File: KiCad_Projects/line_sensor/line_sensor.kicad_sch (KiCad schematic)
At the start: 4 parts, among them J1 Conn_01x05_Female, U1 S4282-51, U2 S4282-51

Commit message: 基盤データのアップデート
ローカルコミットはちゃんと作ってください
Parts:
- removed J1: Conn_01x05_Female, Connector_PinHeader_2.54mm:PinHeader_1x05_P2.54mm_Vertical, symbol Connector:Conn_01x05_Female
- added C1: (no value), symbol Device:C_Small
- added C10, C11, C12, C13, C14, C15, C16, C2, C3, C4, C5, C6, C7, C8, C9: C_Small, symbol Device:C_Small
- added D10, D11, D12, D13, D14, D15, D16, D2, D3, D4, D5, D6, D7, D8, D9: LED, symbol Device:LED
- added J1: (no value), symbol Connector:Conn_01x04_Female
- added U10, U11, U12, U13, U14, U15, U16, U3, U4, U5, U6, U7, U8, U9: S4282-51, symbol New_Library:S4282-51
- D1: value LED -> (none); footprint LED_THT:LED_D3.0mm_Clear -> (none)
- U1, U2: footprint line_sensor:S4282-51 -> (none)
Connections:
- net +5V: now also C1.2, C10.2, C11.2, C12.2, C13.2, C14.2, C15.2, C16.2, C2.2, C3.2, C4.2, C5.2, C6.2, C7.2, C8.2, C9.2, J1.3 (Pin_3), U10.2 (Vcc), U11.2 (Vcc), U12.2 (Vcc), U13.2 (Vcc), U14.2 (Vcc), U15.2 (Vcc), U16.2 (Vcc), U3.2 (Vcc), U4.2 (Vcc), U5.2 (Vcc), U6.2 (Vcc), U7.2 (Vcc), U8.2 (Vcc), U9.2 (Vcc)
- net GND: now also C1.1, C10.1, C11.1, C12.1, C13.1, C14.1, C15.1, C16.1, C2.1, C3.1, C4.1, C5.1, C6.1, C7.1, C8.1, C9.1, J1.2 (Pin_2), U10.4 (GND), U11.4 (GND), U12.4 (GND), U13.4 (GND), U14.4 (GND), U15.4 (GND), U16.4 (GND), U3.4 (GND), U4.4 (GND), U5.4 (GND), U6.4 (GND), U7.4 (GND), U8.4 (GND), U9.4 (GND)
- net 1: now reaches U1.3 (Vout), U2.3 (Vout)
- net 1: now also J1.1 (Pin_1), U10.3 (Vout), U11.3 (Vout), U12.3 (Vout), U13.3 (Vout), U14.3 (Vout), U15.3 (Vout), U16.3 (Vout), U3.3 (Vout), U4.3 (Vout), U5.3 (Vout), U6.3 (Vout), U7.3 (Vout), U8.3 (Vout), U9.3 (Vout)
- net at D1.1 (K): now also U1.1 (K(-))
- new net: D5.1 (K), U5.1 (K(-))
- new net: D12.1 (K), U12.1 (K(-))
- new net: D15.1 (K), U15.1 (K(-))
- new net: D7.1 (K), U7.1 (K(-))
- new net: D3.1 (K), U3.1 (K(-))
- new net: D11.1 (K), U11.1 (K(-))
- new net: D13.1 (K), U13.1 (K(-))
- new net: D2.1 (K), U2.1 (K(-))
- new net: D8.1 (K), U8.1 (K(-))
- new net: D9.1 (K), U9.1 (K(-))
- new net: D16.1 (K), U16.1 (K(-))
- new net: D6.1 (K), U6.1 (K(-))
- new net: D14.1 (K), U14.1 (K(-))
- new net: D10.1 (K), U10.1 (K(-))
- new net: D4.1 (K), U4.1 (K(-))
- new net 5: D1.2 (A), D10.2 (A), D11.2 (A), D12.2 (A), D13.2 (A), D14.2 (A), D15.2 (A), D16.2 (A), D2.2 (A), D3.2 (A), D4.2 (A), D5.2 (A), D6.2 (A), D7.2 (A), D8.2 (A), D9.2 (A), J1.4 (Pin_4)
- no-connect marks 1 -> 0

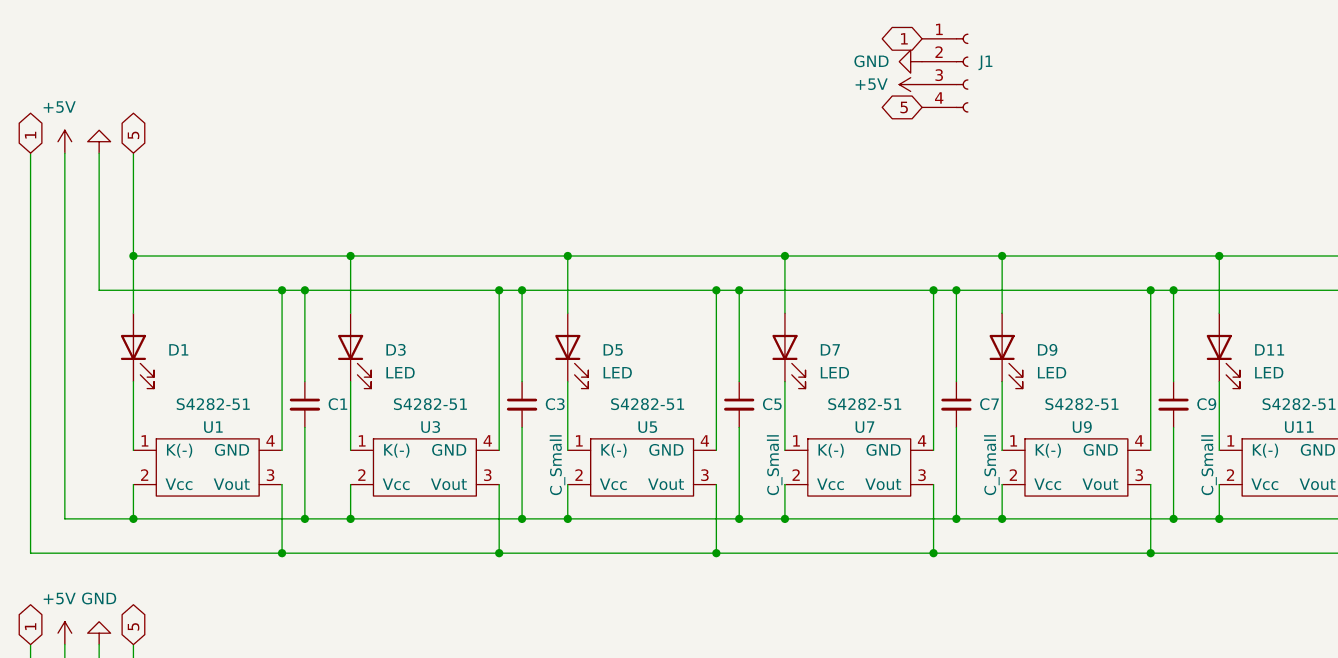
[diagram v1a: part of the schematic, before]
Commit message: 基板データの更新
ラインセンサーの完成
Arduino メイン基板の作成、製作開始。
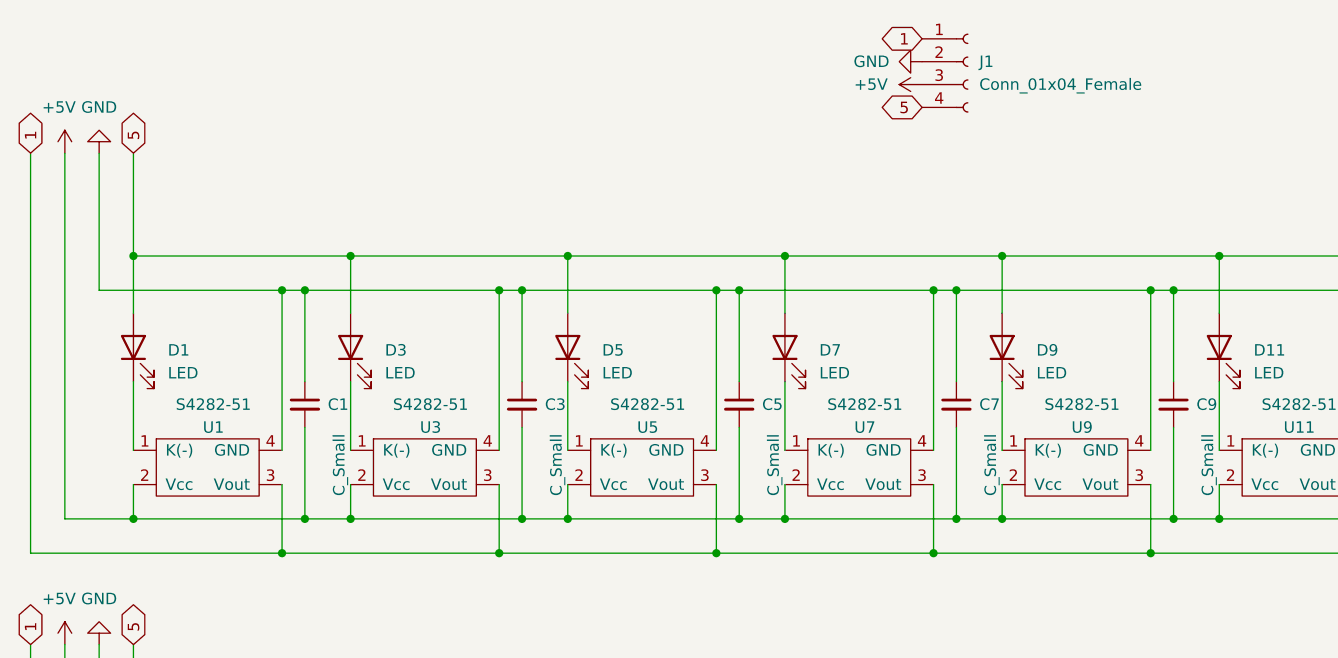
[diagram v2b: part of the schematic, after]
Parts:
- C1: value (none) -> C_Small; footprint (none) -> Capacitor_THT:C_Disc_D3.8mm_W2.6mm_P2.50mm
- C10, C11, C12, C13, C14, C15, C16, C2, C3, C4, C5, C6, C7, C8, C9: footprint (none) -> Capacitor_THT:C_Disc_D3.8mm_W2.6mm_P2.50mm
- D1: value (none) -> LED; footprint (none) -> LED_THT:LED_D3.0mm_Clear
- D10, D11, D12, D13, D14, D15, D16, D2, D3, D4, D5, D6, D7, D8, D9: footprint (none) -> LED_THT:LED_D3.0mm_Clear
- J1: value (none) -> Conn_01x04_Female; footprint (none) -> Connector_PinSocket_2.54mm:PinSocket_1x04_P2.54mm_Vertical
- U1, U10, U11, U12, U13, U14, U15, U16, U2, U3, U4, U5, U6, U7, U8, U9: footprint (none) -> Line_sennsor:Line_sennsor

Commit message: 基板データの更新
IO基板、ライン基板、電源基盤のコネクタ変更、最終確認
メイン基板制作中。
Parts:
- J1: footprint Connector_PinSocket_2.54mm:PinSocket_1x04_P2.54mm_Vertical -> Connector_JST:JST_XH_B4B-XH-A_1x04_P2.50mm_Vertical
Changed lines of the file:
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@@
       (effects (font (size 1.27 1.27)) (justify left))
     )
-    (property "Footprint" "Connector_PinSocket_2.54mm:PinSocket_1x04_P2.54mm_Vertical" (id 2) (at 149.86 48.26 0)
+    (property "Footprint" "Connector_JST:JST_XH_B4B-XH-A_1x04_P2.50mm_Vertical" (id 2) (at 149.86 48.26 0)
       (effects (font (size 1.27 1.27)) hide)
     )
@@
     )
     (path "/99a8bb08-4e59-4c61-8fc9-eb32e2df415d"
-      (reference "J1") (unit 1) (value "Conn_01x04_Female") (footprint "Connector_PinSocket_2.54mm:PinSocket_1x04_P2.54mm_Vertical")
+      (reference "J1") (unit 1) (value "Conn_01x04_Female") (footprint "Connector_JST:JST_XH_B4B-XH-A_1x04_P2.50mm_Vertical")
     )
     (path "/05d6ccc2-421b-4e9d-91cd-1ea66144224c"
